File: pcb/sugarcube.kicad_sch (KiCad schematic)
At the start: 12 parts, among them J1 SIM_Card, U1 nRF9151-LAXX

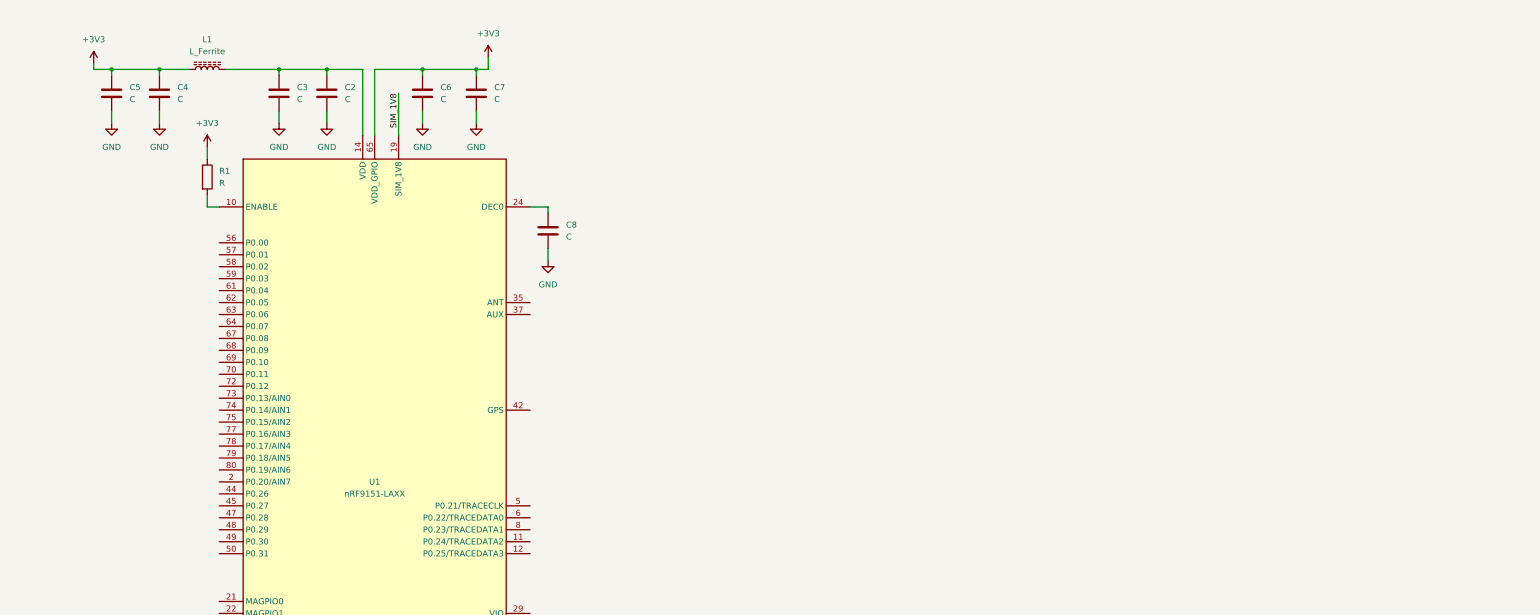
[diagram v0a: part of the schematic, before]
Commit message: Add pmic
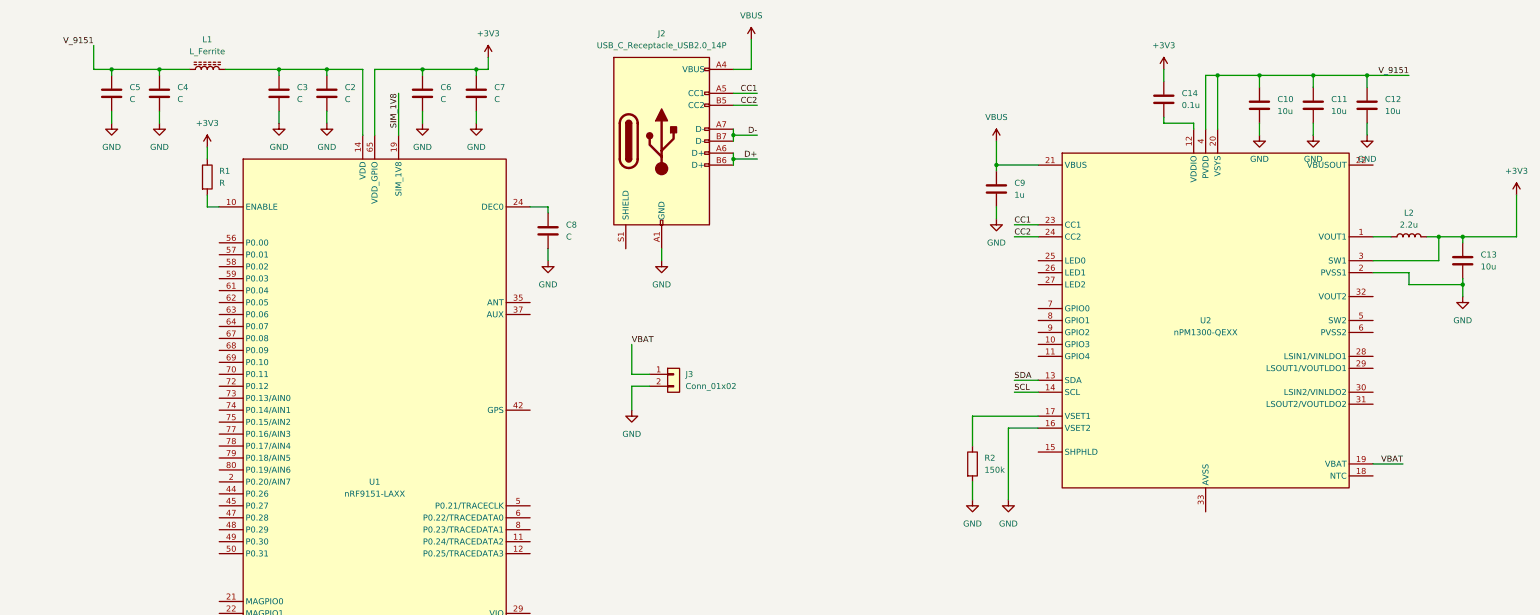
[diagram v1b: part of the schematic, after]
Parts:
- added C10, C11, C12, C13: 10u, symbol Device:C
- added C14: 0.1u, symbol Device:C
- added C9: 1u, symbol Device:C
- added J2: USB_C_Receptacle_USB2.0_14P, symbol Connector:USB_C_Receptacle_USB2.0_14P
- added J3: Conn_01x02, symbol Connector_Generic:Conn_01x02
- added L2: 2.2u, symbol Device:L
- added R2: 150k, symbol Device:R
- added U2: nPM1300-QEXX, Package_DFN_QFN:QFN-32-1EP_5x5mm_P0.5mm_EP3.6x3.6mm_ThermalVias, symbol nordic-lib-kicad-npm:nPM1300-QEXX
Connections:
- net +3V3: now also C13.1, C14.1, L2.2, U2.3 (SW1); no longer C4.1, C5.1, L1.1
- net GND: now also C10.2, C11.2, C12.2, C13.2, C9.2, J2.A1 (GND), J2.A12 (GND), J2.B1 (GND), J2.B12 (GND), J3.2 (Pin_2), R2.2, U2.16 (VSET2), U2.2 (PVSS1)
- new net: L2.1, U2.1 (VOUT1)
- new net: C14.2, U2.12 (VDDIO)
- new net: R2.1, U2.17 (VSET1)
- new net CC1: J2.A5 (CC1), U2.23 (CC1)
- new net CC2: J2.B5 (CC2), U2.24 (CC2)
- new net D+: J2.A6 (D+), J2.B6 (D+)
- new net D-: J2.A7 (D-), J2.B7 (D-)
- new net SCL: U2.14 (SCL)
- new net SDA: U2.13 (SDA)
- new net VBAT: J3.1 (Pin_1), U2.19 (VBAT)
- new net VBUS: C9.1, J2.A4 (VBUS), J2.A9 (VBUS), J2.B4 (VBUS), J2.B9 (VBUS), U2.21 (VBUS)
- new net V_9151: C10.1, C11.1, C12.1, C4.1, C5.1, L1.1, U2.20 (VSYS), U2.4 (PVDD)

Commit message: epd driver
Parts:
- added C15, C16, C17, C19: 1u, symbol Device:C
- added C18, C20: 4.7u, symbol Device:C
- added D1, D2, D3: MBR0530, symbol Device:D
- added J4: Conn_01x24, symbol Connector_Generic:Conn_01x24
- added L3: 47u, symbol Device:L
- added Q1: Q_NMOS, symbol Device:Q_NMOS
- added R3: 1M, symbol Device:R
- added R4: 2.2R, symbol Device:R
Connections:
- net +3V3: now also C16.1, C18.1, J4.15 (Pin_15), J4.16 (Pin_16), L3.1
- net GND: now also C15.1, C16.2, C17.2, C18.2, C19.2, D3.1 (K), J4.17 (Pin_17), J4.8 (Pin_8), R3.2, R4.2
- new net: C20.1, D2.1 (K), D3.2 (A)
- new net: C20.2, D1.2 (A), L3.2, Q1.D
- new net: C17.1, J4.18 (Pin_18)
- new net: C15.2, J4.5 (Pin_5)
- new net BUSY: J4.9 (Pin_9)
- new net CLK: J4.13 (Pin_13)
- new net CS: J4.12 (Pin_12)
- new net D/C: J4.11 (Pin_11)
- new net GDR: J4.2 (Pin_2), Q1.G, R3.1
- new net MOSI: J4.14 (Pin_14)
- new net RES: J4.10 (Pin_10)
- new net RESE: J4.3 (Pin_3), Q1.S, R4.1
- new net VGH: C19.1, D1.1 (K), J4.21 (Pin_21)
- new net VGL: D2.2 (A), J4.23 (Pin_23)

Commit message: More sch
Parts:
- added C21, C22, C23, C24: 1u, symbol Device:C
- added C25, C26, C27, C28, C29, C30, C31, C32, C33, C34, C35, C36: 0.1u, symbol Device:C
- added D10, D11, D4, D5, D6, D7, D8, D9: WS2812B, LED_SMD:LED_WS2812B_PLCC4_5.0x5.0mm_P3.2mm, symbol LED:WS2812B
- added J5: Conn_ARM_SWD_TagConnect_TC2030-NL, Connector:Tag-Connect_TC2030-IDC-NL_2x03_P1.27mm_Vertical, symbol Connector:Conn_ARM_SWD_TagConnect_TC2030-NL
- added J6: Conn_01x02, symbol Connector_Generic:Conn_01x02
- added J7, J8: Conn_01x05, symbol Connector_Generic:Conn_01x05
- added R5, R6: 10k, symbol Device:R
- added SW1, SW2, SW3: SW_Push, symbol Switch:SW_Push
- added U3: W25Q128JVP, Package_SON:WSON-8-1EP_6x5mm_P1.27mm_EP3.4x4.3mm, symbol Memory_Flash:W25Q128JVP
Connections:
- net BUSY is gone; now on net EPD_BUSY: J4.9 (Pin_9)
- net CLK is gone; now on net EPD_SCK: J4.13 (Pin_13)
- net CS is gone; now on net EPD_CS: J4.12 (Pin_12)
- net D/C is gone; now on net EPD_D/C: J4.11 (Pin_11)
- net MOSI is gone; now on net EPD_MOSI: J4.14 (Pin_14)
- net RES is gone; now on net EPD_RES: J4.10 (Pin_10)
- net SCL is gone; now on net PMIC_SCL: U2.14 (SCL)
- net SDA is gone; now on net PMIC_SDA: U2.13 (SDA)
- net +3V3: now also C25.1, C29.1, C30.1, C31.1, C32.1, C33.1, C34.1, C35.1, C36.1, D10.1 (VDD), D11.1 (VDD), D4.1 (VDD), D5.1 (VDD), D6.1 (VDD), D7.1 (VDD), D8.1 (VDD), D9.1 (VDD), R5.1, R6.1, U3.8 (VCC)
- net GND: now also C21.2, C22.2, C23.2, C24.2, C25.2, C26.2, C27.2, C28.2, C29.2, C30.2, C31.2, C32.2, C33.2, C34.2, C35.2, C36.2, D10.3 (VSS), D11.3 (VSS), D4.3 (VSS), D5.3 (VSS), D6.3 (VSS), D7.3 (VSS), D8.3 (VSS), D9.3 (VSS), J5.5 (GND), J7.2 (Pin_2), J8.5 (Pin_5), SW1.1, SW2.1, SW3.1, U3.4 (GND), U3.9 (EP)
- net SWDCLK: now also J5.4 (SWCLK)
- net SWDIO: now also J5.2 (SWDIO)
- net VBAT: now also J6.1 (Pin_1); no longer J3.1 (Pin_1)
- net VBUS: now also J7.1 (Pin_1)
- net VGL: now also C24.1
- net V_9151: now also J5.1 (VCC)
- net nRESET: now also J5.3 (~{RESET})
- net PMIC_INT3: now reaches U2.10 (GPIO3)
- net PMIC_INT4: now reaches U2.11 (GPIO4)
- net PMIC_INT0: now reaches U2.7 (GPIO0)
- net PMIC_INT1: now reaches U2.8 (GPIO1)
- net PMIC_INT2: now reaches U2.9 (GPIO2)
- net RGB_LED: now reaches U1.12 (P0.25/TRACEDATA3)
- net RGB_LED: now also D4.4 (DIN)
- net TEST_2: now reaches U1.2 (P0.20/AIN7)
- net TEST_2: now also J8.2 (Pin_2)
- net TEST_3: now reaches U1.44 (P0.26)
- net TEST_3: now also J8.3 (Pin_3)
- net TEST_4: now reaches U1.45 (P0.27)
- net TEST_4: now also J8.4 (Pin_4)
- net UART_DET: now reaches U1.48 (P0.29)
- net UART_DET: now also J7.5 (Pin_5)
- net UART_TX: now reaches U1.49 (P0.30)
- net UART_TX: now also J7.3 (Pin_3)
- net BUTTON1: now reaches U1.5 (P0.21/TRACECLK)
- net BUTTON1: now also C26.1, SW1.2
- net UART_RX: now reaches U1.50 (P0.31)
- net UART_RX: now also J7.4 (Pin_4)
- net PMIC_SCL: now reaches U1.57 (P0.01)
- net PMIC_SDA: now reaches U1.58 (P0.02)
- net BUTTON2: now reaches U1.6 (P0.22/TRACEDATA0)
- net BUTTON2: now also C27.1, SW2.2
- net FLASH_CS: now reaches U1.61 (P0.04)
- net FLASH_CS: now also U3.1 (~{CS})
- net FLASH_MISO: now reaches U1.62 (P0.05)
- net FLASH_MISO: now also U3.2 (DO/IO_{1})
- net FLASH_SCK: now reaches U1.63 (P0.06)
- net FLASH_SCK: now also U3.6 (CLK)
- net FLASH_MOSI: now reaches U1.64 (P0.07)
- net FLASH_MOSI: now also U3.5 (DI/IO_{0})
- net EPD_BUSY: now reaches U1.67 (P0.08)
- net EPD_RES: now reaches U1.68 (P0.09)
- net EPD_D/C: now reaches U1.69 (P0.10)
- net EPD_CS: now reaches U1.70 (P0.11)
- net EPD_SCK: now reaches U1.73 (P0.13/AIN0)
- net EPD_MOSI: now reaches U1.74 (P0.14/AIN1)
- net BUTTON3: now reaches U1.8 (P0.23/TRACEDATA1)
- net BUTTON3: now also C28.1, SW3.2
- net TEST_1: now reaches U1.80 (P0.19/AIN6)
- net TEST_1: now also J8.1 (Pin_1)
- net at J4.20 (Pin_20): now also C23.1
- net at J4.22 (Pin_22): now also C21.1
- net at J4.24 (Pin_24): now also C22.1
- new net: D4.2 (DOUT), D5.4 (DIN)
- new net: R6.2, U3.3 (~{WP}/IO_{2})
- new net: R5.2, U3.7 (~{HOLD}/~{RESET}/IO_{3})
- new net: J3.1 (Pin_1), J6.2 (Pin_2)
- new net: D10.4 (DIN), D11.2 (DOUT)
- new net: D11.4 (DIN), D7.2 (DOUT)
- new net: D6.2 (DOUT), D7.4 (DIN)
- new net: D10.2 (DOUT), D9.4 (DIN)
- new net: D5.2 (DOUT), D6.4 (DIN)
- new net: D8.4 (DIN), D9.2 (DOUT)
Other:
- note added: "BAT"
- note added: "CHECK"
- note added: "DOCK"
- note added: "I MEAS"
- note added: "RFFE ITF"
- note added: "TEST POINTS"
- moved on the sheet: C15, C16, C17, J3

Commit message: Hierarchical sheets, some docu
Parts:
- removed C1, C2, C3, C4, C5, C6, C7, C8: C, symbol Device:C
- removed C10, C11, C12, C13: 10u, symbol Device:C
- removed C14, C25, C26, C27, C28, C29, C30, C31, C32, C33, C34, C35, C36: 0.1u, symbol Device:C
- removed C15, C16, C17, C19, C21, C22, C23, C24, C9: 1u, symbol Device:C
- removed C18, C20: 4.7u, symbol Device:C
- removed D1, D2, D3: MBR0530, symbol Device:D
- removed D10, D11, D4, D5, D6, D7, D8, D9: WS2812B, LED_SMD:LED_WS2812B_PLCC4_5.0x5.0mm_P3.2mm, symbol LED:WS2812B
- removed J1: SIM_Card, symbol Connector:SIM_Card
- removed J2: USB_C_Receptacle_USB2.0_14P, symbol Connector:USB_C_Receptacle_USB2.0_14P
- removed J3, J6: Conn_01x02, symbol Connector_Generic:Conn_01x02
- removed J4: Conn_01x24, symbol Connector_Generic:Conn_01x24
- removed J5: Conn_ARM_SWD_TagConnect_TC2030-NL, Connector:Tag-Connect_TC2030-IDC-NL_2x03_P1.27mm_Vertical, symbol Connector:Conn_ARM_SWD_TagConnect_TC2030-NL
- removed J7, J8: Conn_01x05, symbol Connector_Generic:Conn_01x05
- removed L1: L_Ferrite, symbol Device:L_Ferrite
- removed L2: 2.2u, symbol Device:L
- removed L3: 47u, symbol Device:L
- removed Q1: Q_NMOS, symbol Device:Q_NMOS
- removed R1: R, symbol Device:R
- removed R2: 150k, symbol Device:R
- removed R3: 1M, symbol Device:R
- removed R4: 2.2R, symbol Device:R
- removed R5, R6: 10k, symbol Device:R
- removed SW1, SW2, SW3: SW_Push, symbol Switch:SW_Push
- removed U1: nRF9151-LAXX, nordic-lib-kicad-nrf9:LGA_9151_12.1x11.1mm, symbol nordic-lib-kicad-nrf9:nRF9151-LAXX
- removed U2: nPM1300-QEXX, Package_DFN_QFN:QFN-32-1EP_5x5mm_P0.5mm_EP3.6x3.6mm_ThermalVias, symbol nordic-lib-kicad-npm:nPM1300-QEXX
- removed U3: W25Q128JVP, Package_SON:WSON-8-1EP_6x5mm_P1.27mm_EP3.4x4.3mm, symbol Memory_Flash:W25Q128JVP
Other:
- added sheet 9151 (9151.kicad_sch)
- added sheet headers (headers.kicad_sch)
- added sheet interface (interface.kicad_sch)
- added sheet power (power.kicad_sch)
- note removed: "BAT"
- note removed: "CHECK"
- note removed: "DOCK"
- note removed: "I MEAS"
- note removed: "RFFE ITF"
- note removed: "TEST POINTS"
- title: (none) -> Sugarcube

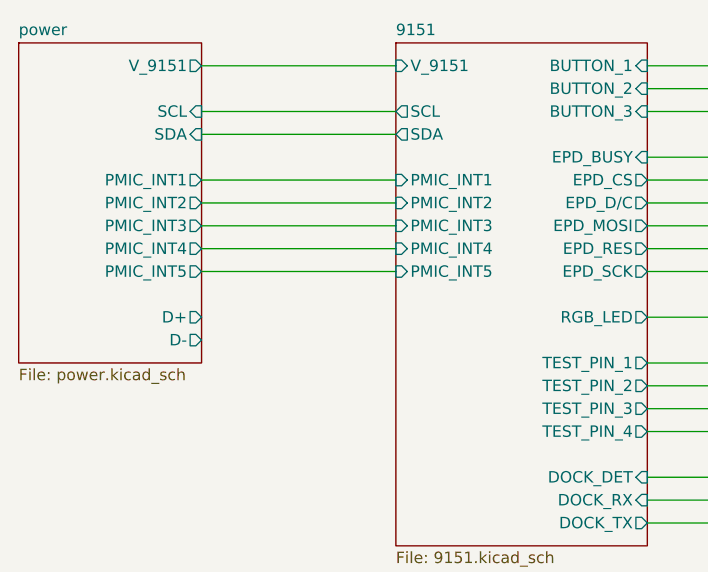
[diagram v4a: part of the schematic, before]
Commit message: Add netclasses and usb-to-uart
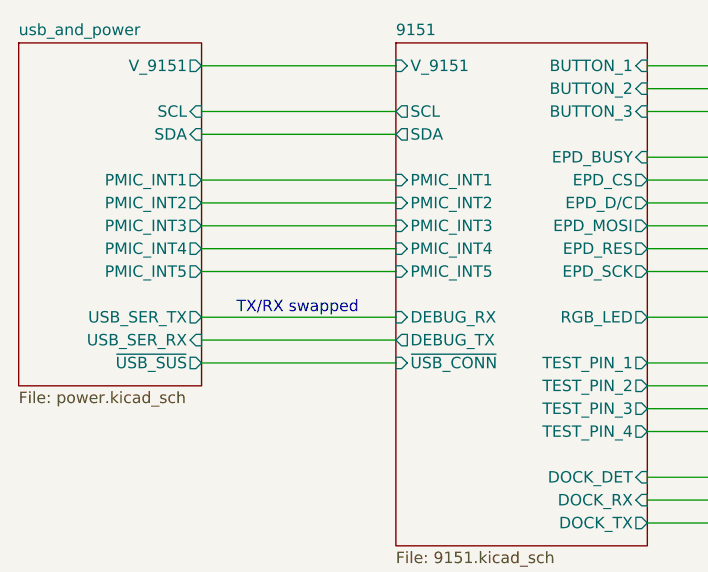
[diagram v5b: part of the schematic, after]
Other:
- sheet power renamed usb_and_power
- sheet 9151 ports: added DEBUG_RX, DEBUG_TX, ~{USB_CONN}; removed none
- sheet usb_and_power ports: added USB_SER_RX, USB_SER_TX, ~{USB_SUS}; removed D+, D-
- note added: "TX/RX swapped"
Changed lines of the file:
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@@
 		(rev "1")
 	)
+	(text "TX/RX swapped\n"
+		(exclude_from_sim no)
+		(at 119.888 92.964 0)
+		(effects
+			(font
+				(size 1.27 1.27)
+				(color 0 5 255 1)
+			)
+		)
+	)
 	(wire
 		(pts
@@
 	(wire
 		(pts
+			(xy 109.22 93.98) (xy 130.81 93.98)
+		)
+		(stroke
+			(width 0)
+			(type default)
+		)
+	)
+	(wire
+		(pts
 			(xy 109.22 83.82) (xy 130.81 83.82)
 		)
@@
 	(wire
 		(pts
+			(xy 109.22 96.52) (xy 130.81 96.52)
+		)
+		(stroke
+			(width 0)
+			(type default)
+		)
+	)
+	(wire
+		(pts
 			(xy 158.75 88.9) (xy 180.34 88.9)
 		)
@@
 		(pts
 			(xy 171.45 113.03) (xy 171.45 106.68)
+		)
+		(stroke
+			(width 0)
+			(type default)
+		)
+	)
+	(wire
+		(pts
+			(xy 109.22 99.06) (xy 130.81 99.06)
 		)
 		(stroke
@@
 	(sheet
 		(at 88.9 63.5)
-		(size 20.32 35.56)
+		(size 20.32 38.1)
 		(exclude_from_sim no)
 		(in_bom yes)
@@
 			(color 0 0 0 0.0000)
 		)
-		(property "Sheetname" "power"
+		(property "Sheetname" "usb_and_power"
 			(at 88.9 62.7884 0)
 			(effects
@@
 		)
 		(property "Sheetfile" "power.kicad_sch"
-			(at 88.9 99.6446 0)
+			(at 88.9 102.1846 0)
 			(effects
 				(font
@@
 				)
 				(justify left top)
-			)
-		)
-		(pin "D+" output
-			(at 109.22 93.98 0)
-			(effects
-				(font
-					(size 1.27 1.27)
-				)
-				(justify right)
-			)
-		)
-		(pin "D-" output
-			(at 109.22 96.52 0)
-			(effects
-				(font
-					(size 1.27 1.27)
-				)
-				(justify right)
 			)
 		)
@@
 		(pin "SDA" input
 			(at 109.22 73.66 0)
+			(effects
+				(font
+					(size 1.27 1.27)
+				)
+				(justify right)
+			)
+		)
+		(pin "USB_SER_TX" output
+			(at 109.22 93.98 0)
+			(effects
+				(font
+					(size 1.27 1.27)
+				)
+				(justify right)
+			)
+		)
+		(pin "USB_SER_RX" input
+			(at 109.22 96.52 0)
+			(effects
+				(font
+					(size 1.27 1.27)
+				)
+				(justify right)
+			)
+		)
+		(pin "~{USB_SUS}" output
+			(at 109.22 99.06 0)
 			(effects
 				(font
@@
 			(effects
 				(font
+					(size 1.27 1.27)
+				)
+				(justify left)
+			)
+		)
+		(pin "DEBUG_RX" input
+			(at 130.81 93.98 180)
+			(effects
+				(font
+					(size 1.27 1.27)
+				)
+				(justify left)
+			)
+		)
+		(pin "DEBUG_TX" output
+			(at 130.81 96.52 180)
+			(effects
+				(font
+					(size 1.27 1.27)
+				)
+				(justify left)
+			)
+		)
+		(pin "~{USB_CONN}" input
+			(at 130.81 99.06 180)
+			(effects
+				(font

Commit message: Adding filters
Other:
- sheet 9151 renamed nRF9151
- sheet headers renamed Headers
- sheet interface renamed Interface
- sheet usb_and_power renamed PMIC
- added sheet Battery (battery.kicad_sch)
- added sheet USB (usb.kicad_sch)
- sheet PMIC ports: added VBAT, VBUS; removed USB_SER_RX, USB_SER_TX, ~{USB_SUS}
- note added: "Controller"
- note added: "Power Supply"
- note added: "User Interface"
